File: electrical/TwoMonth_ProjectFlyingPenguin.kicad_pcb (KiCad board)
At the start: 2 copper layers, 10 parts, among them J1 USB_B_Micro, J2 SWD, J3 Micro_SD_Card_Det, M1 Elevator_Servo, M2 Fin_Servo, U1 ATSAMD21G18A-AUT, U2 AT25SF081-XMHD-X, U3 BNO055, U4 MS561101BA03-50, Y1 Crystal

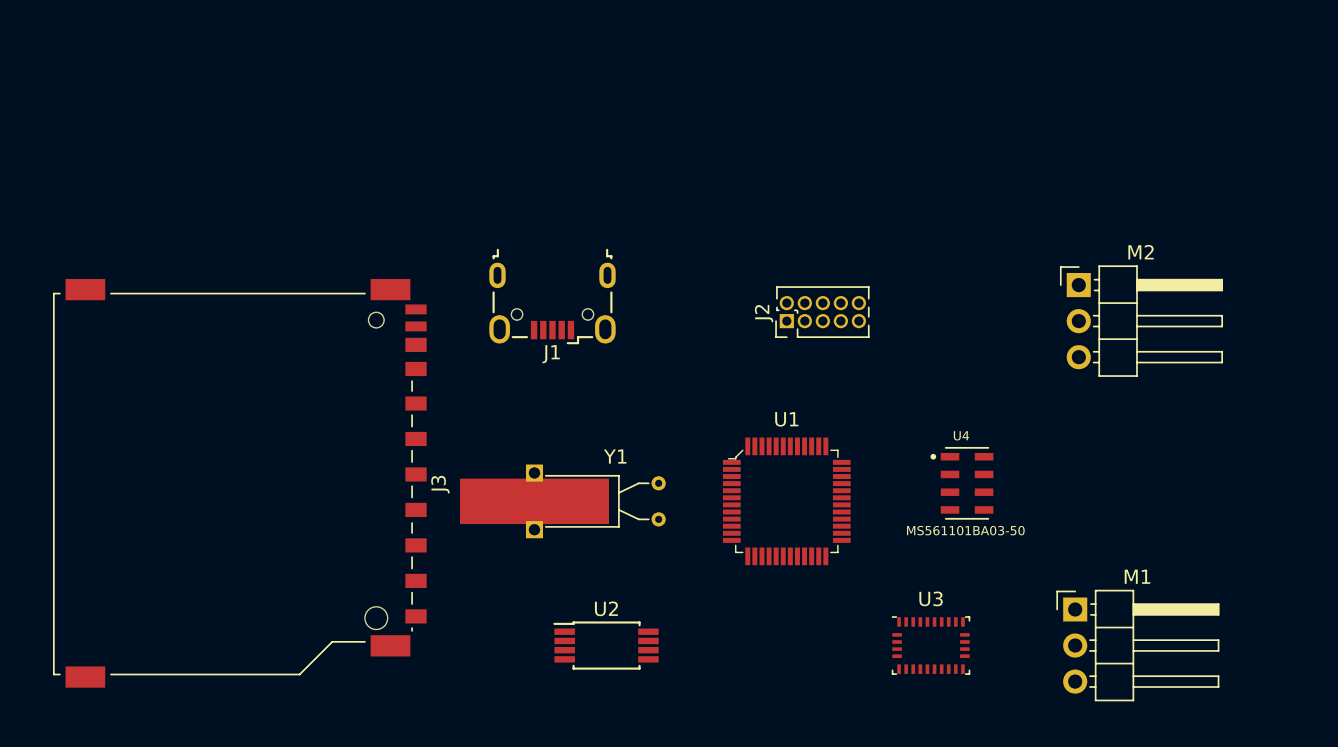
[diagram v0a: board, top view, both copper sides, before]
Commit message: Finished placing parts. need to route tracks
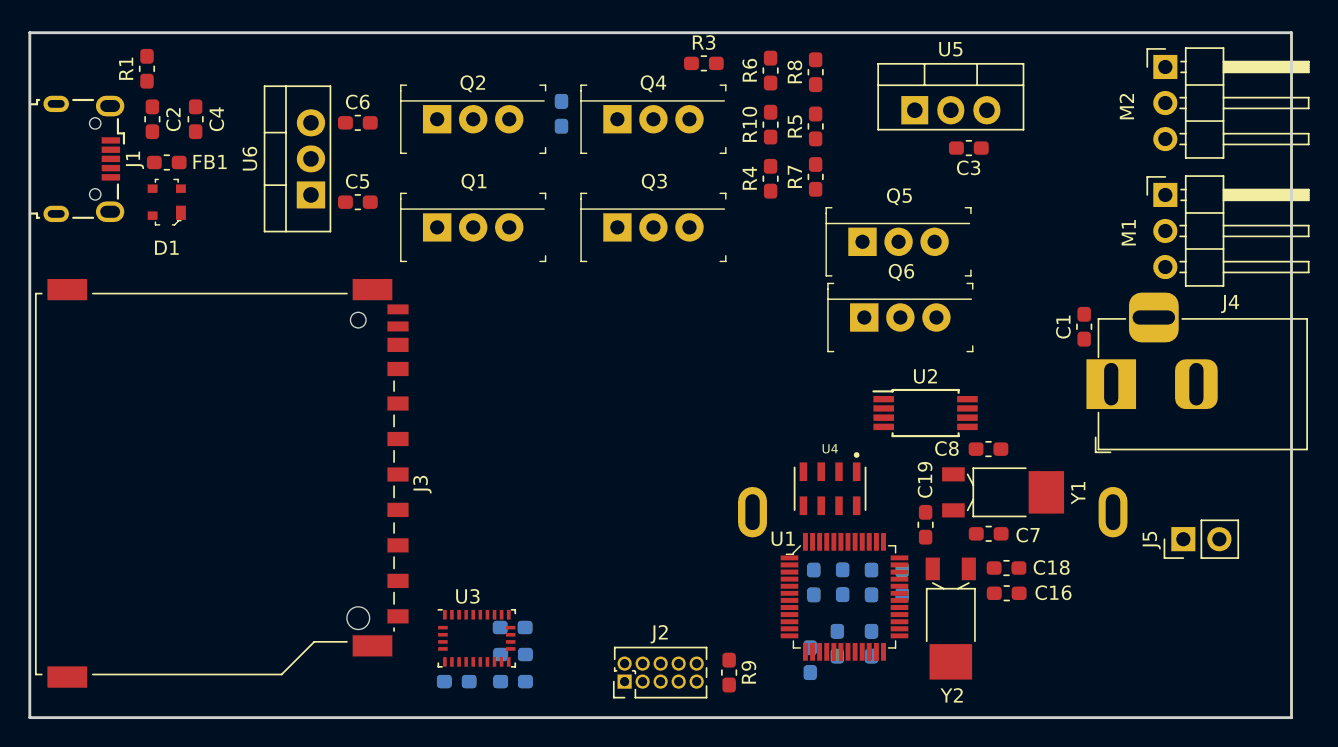
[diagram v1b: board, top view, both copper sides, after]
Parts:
- added C1: 0.47uF, Capacitor_SMD:C_0603_1608Metric_Pad1.05x0.95mm_HandSolder, F.Cu at (167.0, 44.8)
- added C10: 100nF, Capacitor_SMD:C_0603_1608Metric_Pad1.05x0.95mm_HandSolder, B.Cu at (150.0, 62.9)
- added C11: 1uF, Capacitor_SMD:C_0603_1608Metric_Pad1.05x0.95mm_HandSolder, B.Cu at (152.0, 62.9)
- added C12: 100nF, Capacitor_SMD:C_0603_1608Metric_Pad1.05x0.95mm_HandSolder, B.Cu at (154.2, 62.9)
- added C13: 100nF, Capacitor_SMD:C_0603_1608Metric_Pad1.05x0.95mm_HandSolder, B.Cu at (149.6, 67.2)
- added C14: 10uF, Capacitor_SMD:C_0603_1608Metric_Pad1.05x0.95mm_HandSolder, B.Cu at (148.0, 62.9)
- added C15: 100nF, Capacitor_SMD:C_0603_1608Metric_Pad1.05x0.95mm_HandSolder, B.Cu at (147.7, 68.3)
- added C16: 0.1uF, Capacitor_SMD:C_0603_1608Metric_Pad1.05x0.95mm_HandSolder, F.Cu at (161.5, 63.6)
- added C17: 0.1uF, Capacitor_SMD:C_0603_1608Metric_Pad1.05x0.95mm_HandSolder, B.Cu at (126.8, 69.8)
- added C18: 22pF, Capacitor_SMD:C_0603_1608Metric_Pad1.05x0.95mm_HandSolder, F.Cu at (161.5, 61.8)
- added C19: 22pF, Capacitor_SMD:C_0603_1608Metric_Pad1.05x0.95mm_HandSolder, F.Cu at (155.8, 58.8)
- added C2: 1nF, Capacitor_SMD:C_0603_1608Metric_Pad1.05x0.95mm_HandSolder, F.Cu at (101.3, 30.2)
- added C3: 22uF, Capacitor_SMD:C_0603_1608Metric_Pad1.05x0.95mm_HandSolder, F.Cu at (158.9, 32.3)
- added C4: 1nF, Capacitor_SMD:C_0603_1608Metric_Pad1.05x0.95mm_HandSolder, F.Cu at (104.4, 30.2)
- added C5: 10uF, Capacitor_SMD:C_0603_1608Metric_Pad1.05x0.95mm_HandSolder, F.Cu at (115.8, 36.1)
- added C6: 10uF, Capacitor_SMD:C_0603_1608Metric_Pad1.05x0.95mm_HandSolder, F.Cu at (115.8, 30.5)
- added C7: 6.8pF, Capacitor_SMD:C_0603_1608Metric_Pad1.05x0.95mm_HandSolder, F.Cu at (160.3, 59.4)
- added C8: 6.8pF, Capacitor_SMD:C_0603_1608Metric_Pad1.05x0.95mm_HandSolder, F.Cu at (160.3, 53.5)
- added C9: 4F, Battery:SuperCap, B.Cu at (156.3, 57.9)
- added D1: PRTR5V0U2X_215, digikey-footprints:TO-253-4, F.Cu at (102.4, 36.1)
- added FB1: 470 @ 100Mhz (BLM18PG471SN1), Capacitor_SMD:C_0603_1608Metric_Pad1.05x0.95mm_HandSolder, F.Cu at (102.4, 33.3)
- added FB2: 470 @ 100Mhz (BLM18PG471SN1), Capacitor_SMD:C_0603_1608Metric_Pad1.05x0.95mm_HandSolder, B.Cu at (152.0, 67.2)
- added J4: Battery_Barrel_Jack, Connector_BarrelJack:BarrelJack_Horizontal, F.Cu at (168.9, 48.9)
- added J5: Hotwire, Connector_PinHeader_2.54mm:PinHeader_1x02_P2.54mm_Vertical, F.Cu at (174.0, 59.8)
- added Q1: PFETDefaultA, digikey-footprints:TO-220-3, F.Cu at (121.4, 37.8)
- added Q2: PFETAltA, digikey-footprints:TO-220-3, F.Cu at (121.4, 30.2)
- added Q3: PFETDefaultB, digikey-footprints:TO-220-3, F.Cu at (134.1, 37.8)
- added Q4: PFETAltB, digikey-footprints:TO-220-3, F.Cu at (134.1, 30.2)
- added Q5: FQP27P06, digikey-footprints:TO-220-3, F.Cu at (151.4, 38.9)
- added Q6: FQP30N06L, digikey-footprints:TO-220-3, F.Cu at (151.5, 44.2)
- added R1: 200K, Resistor_SMD:R_0603_1608Metric_Pad1.05x0.95mm_HandSolder, F.Cu at (101.0, 26.7)
- added R10: 10k, Resistor_SMD:R_0603_1608Metric_Pad1.05x0.95mm_HandSolder, F.Cu at (144.9, 30.6)
- added R11: 10k, Resistor_SMD:R_0603_1608Metric_Pad1.05x0.95mm_HandSolder, B.Cu at (122.8, 69.8)
- added R12: 10k, Resistor_SMD:R_0603_1608Metric_Pad1.05x0.95mm_HandSolder, B.Cu at (126.7, 66.0)
- added R13: 10k, Resistor_SMD:R_0603_1608Metric_Pad1.05x0.95mm_HandSolder, B.Cu at (126.8, 67.9)
- added R2: 200K, Resistor_SMD:R_0603_1608Metric_Pad1.05x0.95mm_HandSolder, B.Cu at (130.2, 29.8)
- added R3: 100K, Resistor_SMD:R_0603_1608Metric_Pad1.05x0.95mm_HandSolder, F.Cu at (140.2, 26.3)
- added R4: 10k, Resistor_SMD:R_0603_1608Metric_Pad1.05x0.95mm_HandSolder, F.Cu at (144.9, 34.4)
- added R5: 10k, Resistor_SMD:R_0603_1608Metric_Pad1.05x0.95mm_HandSolder, F.Cu at (148.1, 30.7)
- added R6: 10k, Resistor_SMD:R_0603_1608Metric_Pad1.05x0.95mm_HandSolder, F.Cu at (144.9, 26.8)
- added R7: 10k, Resistor_SMD:R_0603_1608Metric_Pad1.05x0.95mm_HandSolder, F.Cu at (148.1, 34.3)
- added R8: 10k, Resistor_SMD:R_0603_1608Metric_Pad1.05x0.95mm_HandSolder, F.Cu at (148.1, 26.9)
- added R9: 1k, Resistor_SMD:R_0603_1608Metric_Pad1.05x0.95mm_HandSolder, F.Cu at (142.0, 69.2)
- added U5: LM2940_TO220, Package_TO_SOT_THT:TO-220-3_Vertical, F.Cu at (155.1, 29.6)
- added U6: MIC29310, Package_TO_SOT_THT:TO-220-3_Vertical, F.Cu at (112.5, 35.6)
- added Y2: 32.768Khz, Crystal:Crystal_SMD_MicroCrystal_MS1V-T1K, F.Cu at (157.6, 65.4)
- J2: value SWD -> Conn_ARM_JTAG_SWD_10
- Y1: value Crystal -> 32.768Khz; footprint Crystal:Crystal_AT310_D3.0mm_L10.0mm_Horizontal_1EP_style2 -> Crystal:Crystal_SMD_MicroCrystal_MS1V-T1K
- moved J1 34.5 mm to (96.5, 33.0), turned to 270 degrees
- moved U3 32.0 mm to (124.2, 66.8)
- moved M1 29.9 mm to (172.7, 35.6)
- moved J2 27.9 mm to (134.6, 69.8)
- moved U2 27.8 mm to (155.8, 50.9)
- moved Y1 24.3 mm to (161.3, 56.5), turned to 90 degrees
- moved M2 16.5 mm to (172.7, 26.5)
- moved U4 9.66 mm to (149.1, 56.3), turned to 270 degrees
- moved U1 7.86 mm to (150.1, 63.9)
- moved J3 1.27 mm to (106.7, 55.9)
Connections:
- net Net-(J2-Pad10) renamed /~SYS_RESET
- net Net-(U1-Pad3) renamed /BATTV_ADC0
- net Net-(U1-Pad37) renamed /FLIGHT_LED_2
- net Net-(U1-Pad4) renamed /THERM1_ADC1
- net Net-(U1-Pad7) renamed /FLIGHT_LED_0
- net Net-(U1-Pad8) renamed /FLIGHT_LED_1
- net Net-(U1-Pad9) renamed /SPI0_MISO
- J1 pad 1: Net-(J1-Pad1) -> /VBUS
- J1 pad 2: Net-(J1-Pad2) -> /USB_D-
- J1 pad 3: Net-(J1-Pad3) -> /USB_D+
- J1 pad 5: Net-(J1-Pad5) -> GND
- J1 pad 6: Net-(J1-Pad6) -> GND
- J2 pad 1: Net-(J2-Pad1) -> +3V3
- J2 pad 2: Net-(J2-Pad2) -> /SWDIO
- J2 pad 3: Net-(J2-Pad3) -> GND
- J2 pad 4: Net-(J2-Pad4) -> /SWCLK
- J2 pad 5: Net-(J2-Pad3) -> GND
- J2 pad 9: Net-(J2-Pad9) -> GND
- J3 pad 10: Net-(J3-Pad10) -> /uSD_CARD_DET
- J3 pad 11: Net-(J3-Pad11) -> GND
- J3 pad 2: Net-(J3-Pad2) -> /SPI0_SS_1
- J3 pad 3: Net-(J3-Pad3) -> /SPI0_MOSI
- J3 pad 4: Net-(J3-Pad4) -> +3V3
- J3 pad 5: Net-(J3-Pad5) -> /SPI0_SCK
- J3 pad 6: Net-(J3-Pad6) -> GND
- J3 pad 7: Net-(J3-Pad7) -> /SPI0_MOSI
- M1 pad 1: Net-(M1-Pad1) -> /PWM1_ELEV
- M1 pad 2: Net-(M1-Pad2) -> +5V
- M1 pad 3: Net-(M1-Pad3) -> GND
- M2 pad 1: Net-(M2-Pad1) -> /PWM0_FIN
- M2 pad 2: Net-(M2-Pad2) -> +5V
- M2 pad 3: Net-(M2-Pad3) -> GND
- U1 pad 1: Net-(U1-Pad1) -> /XIN32
- U1 pad 10: Net-(U1-Pad10) -> /SPI0_SS_0
- U1 pad 11: Net-(U1-Pad11) -> /SPI0_MOSI
- U1 pad 12: Net-(U1-Pad12) -> /SPI0_SCK
- U1 pad 13: Net-(U1-Pad13) -> /SDA
- U1 pad 14: Net-(U1-Pad14) -> /SCL
- U1 pad 15: Net-(U1-Pad15) -> /PWM1_ELEV
- U1 pad 16: Net-(U1-Pad16) -> /Hotwire_GPO
- U1 pad 17: Net-(U1-Pad17) -> +3V3
- U1 pad 18: Net-(U1-Pad18) -> GND
- U1 pad 19: Net-(U1-Pad19) -> /PWM0_FIN
- U1 pad 2: Net-(U1-Pad2) -> /XOUT32
- U1 pad 21: Net-(U1-Pad21) -> /SPI0_SS_1
- U1 pad 22: Net-(U1-Pad22) -> /uSD_CARD_DET
- U1 pad 33: Net-(U1-Pad33) -> /USB_D-
- U1 pad 34: Net-(U1-Pad34) -> /USB_D+
- U1 pad 35: Net-(U1-Pad35) -> GND
- U1 pad 36: Net-(U1-Pad36) -> +3V3
- U1 pad 40: Net-(U1-Pad40) -> /~MCU_RESET
- U1 pad 42: Net-(U1-Pad42) -> GND
- U1 pad 43: Net-(U1-Pad43) -> +3V3
- U1 pad 44: Net-(U1-Pad44) -> +3V3
- U1 pad 45: Net-(U1-Pad45) -> /SWCLK
- U1 pad 46: Net-(U1-Pad46) -> /SWDIO
- U1 pad 5: Net-(U1-Pad5) -> GND
- U1 pad 6: Net-(U1-Pad6) -> /VDD_ANA
- U2 pad 1: Net-(U2-Pad1) -> /SPI0_SS_0
- U2 pad 2: Net-(U2-Pad2) -> /SPI0_MOSI
- U2 pad 4: Net-(U2-Pad4) -> GND
- U2 pad 5: Net-(U2-Pad5) -> /SPI0_MOSI
- U2 pad 6: Net-(U2-Pad6) -> /SPI0_SCK
- U2 pad 8: Net-(U2-Pad8) -> +3V3
- U3 pad 10: Net-(U3-Pad10) -> GND
- U3 pad 11: Net-(U3-Pad11) -> /~MCU_RESET
- U3 pad 15: Net-(U3-Pad15) -> GND
- U3 pad 16: Net-(U3-Pad15) -> GND
- U3 pad 18: Net-(U3-Pad18) -> GND
- U3 pad 19: Net-(U3-Pad19) -> /SCL
- U3 pad 2: Net-(U3-Pad2) -> GND
- U3 pad 20: Net-(U3-Pad20) -> /SDA
- U3 pad 25: Net-(U3-Pad15) -> GND
- U3 pad 26: Net-(U3-Pad26) -> /BNO_XOUT32
- U3 pad 27: Net-(U3-Pad27) -> /BNO_XIN32
- U3 pad 28: Net-(U3-Pad28) -> +3V3
- U3 pad 3: Net-(U3-Pad3) -> +3V3
- U3 pad 4: Net-(U3-Pad4) -> +3V3
- U4 pad 1: Net-(U4-Pad1) -> +3V3
- U4 pad 2: Net-(U4-Pad2) -> Net-(R10-Pad1)
- U4 pad 3: Net-(U4-Pad3) -> GND
- U4 pad 4: Net-(U4-Pad4) -> Net-(R10-Pad1)
- U4 pad 5: Net-(U4-Pad4) -> Net-(R10-Pad1)
- U4 pad 7: Net-(U4-Pad7) -> /SDA
- U4 pad 8: Net-(U4-Pad8) -> /SCL
- Y1 pad 1: Net-(Y1-Pad1) -> /XIN32
- Y1 pad 2: Net-(Y1-Pad2) -> /XOUT32
- Y1 pad 3: (no net) -> GND
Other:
- board outline added: 88.9 x 48.3 mm

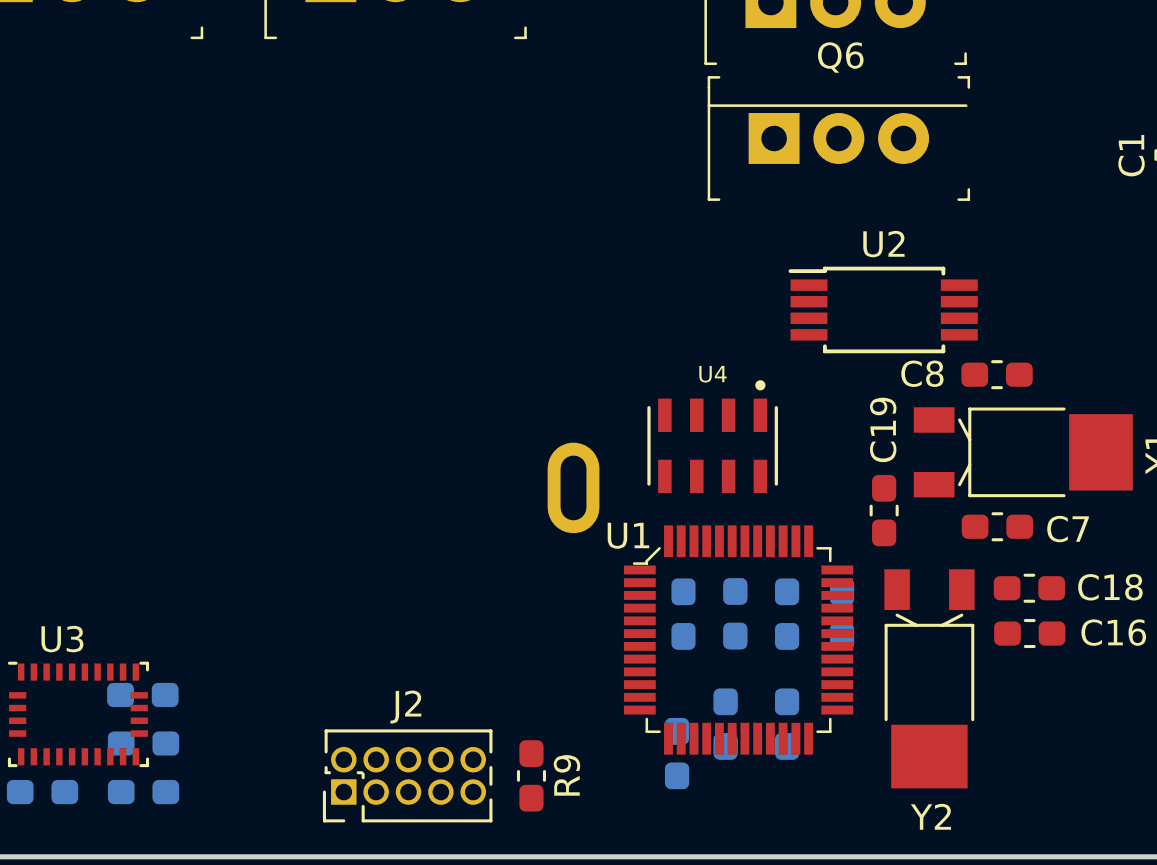
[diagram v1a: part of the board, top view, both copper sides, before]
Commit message: Finished schematic I think. Cant find part for rbf switch
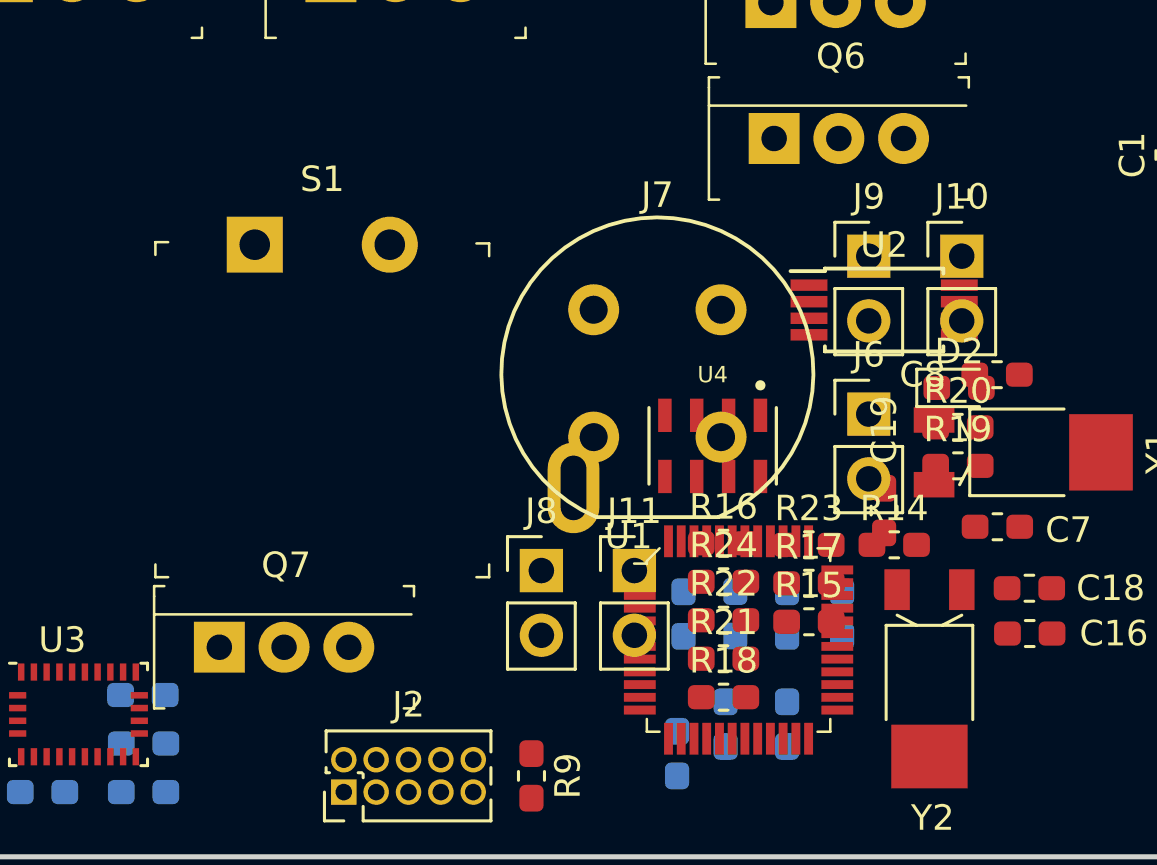
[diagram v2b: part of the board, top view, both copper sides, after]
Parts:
- added D2: POWER_LED, LED_SMD:LED_0603_1608Metric_Pad1.05x0.95mm_HandSolder, F.Cu at (158.8, 54.0)
- added J10: NTCLE100E3103JB0 (Therm 1), Connector_PinHeader_2.54mm:PinHeader_1x02_P2.54mm_Vertical, F.Cu at (158.9, 48.8)
- added J11: NTCLE100E3103JB0 (Therm 2), Connector_PinHeader_2.54mm:PinHeader_1x02_P2.54mm_Vertical, F.Cu at (146.0, 61.2)
- added J6: FLIGHT_LED_0, Connector_PinHeader_2.54mm:PinHeader_1x02_P2.54mm_Vertical, F.Cu at (155.2, 55.0)
- added J7: SS0750301F020P1A, Button_Switch_THT:Push_E-Switch_KS01Q01, F.Cu at (144.4, 50.9)
- added J8: FLIGHT_LED_1, Connector_PinHeader_2.54mm:PinHeader_1x02_P2.54mm_Vertical, F.Cu at (142.4, 61.2)
- added J9: FLIGHT_LED_2, Connector_PinHeader_2.54mm:PinHeader_1x02_P2.54mm_Vertical, F.Cu at (155.2, 48.8)
- added Q7: FQP30N06L, digikey-footprints:TO-220-3, F.Cu at (129.7, 64.2)
- added R14: 330, Resistor_SMD:R_0603_1608Metric_Pad1.05x0.95mm_HandSolder, F.Cu at (156.2, 60.1)
- added R15: 25, Resistor_SMD:R_0603_1608Metric_Pad1.05x0.95mm_HandSolder, F.Cu at (152.9, 63.2)
- added R16: 4.7k, Resistor_SMD:R_0603_1608Metric_Pad1.05x0.95mm_HandSolder, F.Cu at (149.5, 60.1)
- added R17: 25, Resistor_SMD:R_0603_1608Metric_Pad1.05x0.95mm_HandSolder, F.Cu at (152.9, 61.7)
- added R18: 25, Resistor_SMD:R_0603_1608Metric_Pad1.05x0.95mm_HandSolder, F.Cu at (149.5, 66.1)
- added R19: 100k, Resistor_SMD:R_0603_1608Metric_Pad1.05x0.95mm_HandSolder, F.Cu at (158.7, 57.0)
- added R20: 39, Resistor_SMD:R_0603_1608Metric_Pad1.05x0.95mm_HandSolder, F.Cu at (158.7, 55.5)
- added R21: 10k, Resistor_SMD:R_0603_1608Metric_Pad1.05x0.95mm_HandSolder, F.Cu at (149.5, 64.6)
- added R22: 3.2k, Resistor_SMD:R_0603_1608Metric_Pad1.05x0.95mm_HandSolder, F.Cu at (149.5, 63.1)
- added R23: 20k, Resistor_SMD:R_0603_1608Metric_Pad1.05x0.95mm_HandSolder, F.Cu at (152.9, 60.1)
- added R24: 20k, Resistor_SMD:R_0603_1608Metric_Pad1.05x0.95mm_HandSolder, F.Cu at (149.5, 61.6)
- added S1: ~RESET_BUTTON, digikey-footprints:PushButton_12x12mm_THT_GPTS203211B, F.Cu at (131.1, 48.4)
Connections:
- net /FLIGHT_LED_1 renamed Net-(U1-Pad8)
- C1 pad 1: Net-(C1-Pad1) -> /RAW_BATTERY_V+
- J4 pad 1: Net-(C1-Pad1) -> Net-(J4-Pad1)
- U1 pad 37: /FLIGHT_LED_2 -> /FLIGHT_LED_CTRL
- U1 pad 40: /~MCU_RESET -> /~SYS_RESET
- U1 pad 7: /FLIGHT_LED_0 -> /THERM2_ADC2
- U3 pad 11: /~MCU_RESET -> /~SYS_RESET
- U5 pad 1: Net-(C1-Pad1) -> /RAW_BATTERY_V+
- Y2 pad 3: Net-(Y2-Pad3) -> GND
